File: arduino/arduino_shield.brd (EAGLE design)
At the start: 100 x 80 mm, 14 parts, among them IC3 PCF8574T, IC4 PCF8574T

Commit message: Board erstellt
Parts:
- removed C1: (no value), rcl:C0805
- removed JP6: (no value), pinheader_250:1X10
- added LED1, LED2, LED3: (no value), adafruit:CHIP-LED0805
- added R3, R4, R5: (no value), resistor:R0805
- added SG1: F/HGP, buzzer:F/HGP
- added U$1: (no value), frames:A4L-LOC
- JP1: value (none) -> POWERCON; device pinheader_250:1X03 -> PowerCon:AYAB_POW
- JP5: device pinheader_250:1X05 -> pinheader_250:1X10
- moved JP1 59.7 mm to (14.0, 21.6), turned to 90 degrees
- moved R1 37.6 mm to (41.3, 21.3), flipped to the bottom, turned to 270 degrees
- moved R2 35.2 mm to (41.3, 25.4), flipped to the bottom, turned to 90 degrees
- moved IC4 15.4 mm to (54.0, 26.0), flipped to the bottom, turned to 90 degrees
- moved JP3 14.7 mm to (53.3, 49.2)
- moved IC2 14.5 mm to (54.6, 40.6)
- moved IC3 13.0 mm to (29.2, 26.0), flipped to the bottom, turned to 90 degrees
- moved JP4 12.4 mm to (26.0, 49.2)
- moved IC1 12.1 mm to (29.8, 40.6)
- moved ARD1 8.89 mm to (8.89, 14.0)
- moved JP5 8.89 mm to (72.4, 35.6), turned to 270 degrees
- moved JP2 4.13 mm to (64.8, 21.3), turned to 180 degrees
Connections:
- net EOL_R renamed EOL0L
- removed net 5V: ARD1.5V
- removed net AREF: ARD1.AREF
- removed net EOL_L: ARD1.AIN0, JP1.1
- removed net GND1: ARD1.GND@1, ARD1.GND@2, ARD1.GND@3, C1.2, IC1.9, IC2.9, IC3.1, IC3.2, IC3.3, IC3.8, IC4.2, IC4.3, IC4.8, JP1.2, JP2.2, JP5.4, JP6.7
- removed net INT0: ARD1.2
- removed net INT1: ARD1.3
- removed net V+: IC1.10, IC2.10, JP4.1, JP4.2, JP6.10
- new net +15V: IC1.10, IC2.10, JP1.P$1, JP4.1, JP4.2
- new net +5V/1: JP1.P$4
- new net ENC0PINA: ARD1.2, JP5.4
- new net ENC0PINB: ARD1.3, JP5.5
- new net ENC0PINC: ARD1.4, JP5.6
- new net EOL0R: ARD1.AIN0, JP5.8
- new net GND: ARD1.GND@1, ARD1.GND@2, ARD1.GND@3, IC1.9, IC2.9, IC3.1, IC3.2, IC3.3, IC3.8, IC4.2, IC4.3, IC4.8, JP1.P$2, JP1.P$3, JP2.2, JP5.10, JP5.2, JP5.7, JP5.9, LED1.C
- new net N$33: LED1.A, R3.1
- new net N$34: ARD1.9, SG1.1
- new net N$35: ARD1.6, LED3.C
- new net N$36: ARD1.5, LED2.C
- new net N$37: LED3.A, R4.2
- new net N$38: LED2.A, R5.2
- net +5V: now also ARD1.5V, ARD1.AREF, IC4.1, JP5.1, R3.2, R4.1, R5.1, SG1.2; no longer C1.1, JP1.3, JP5.5, JP6.3
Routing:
- net +15V: track 0.00 -> 82.1 mm
- net SCL: track 0.00 -> 49.5 mm
- net GND: track 0.00 -> 48.2 mm, vias 0 -> 1
- net SDA: track 0.00 -> 46.3 mm
- net N$34: track 0.00 -> 36.2 mm
- net ENC0PINC: track 0.00 -> 35.4 mm
- net ENC0PINB: track 0.00 -> 31.8 mm
- net ENC0PINA: track 0.00 -> 28.1 mm
- net EOL0R: track 0.00 -> 23.4 mm
- net N$2: track 0.00 -> 15.1 mm
- net N$1: track 0.00 -> 15.1 mm
- net N$16: track 0.00 -> 14.1 mm
- net N$9: track 0.00 -> 14.1 mm
- net N$3: track 0.00 -> 13.9 mm
- net N$10: track 0.00 -> 13.9 mm
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- added copper zone on layer 16, net +5V
- added copper zone on layer 1, net GND
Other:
- board size 100 x 80 mm -> 69.2 x 54 mm

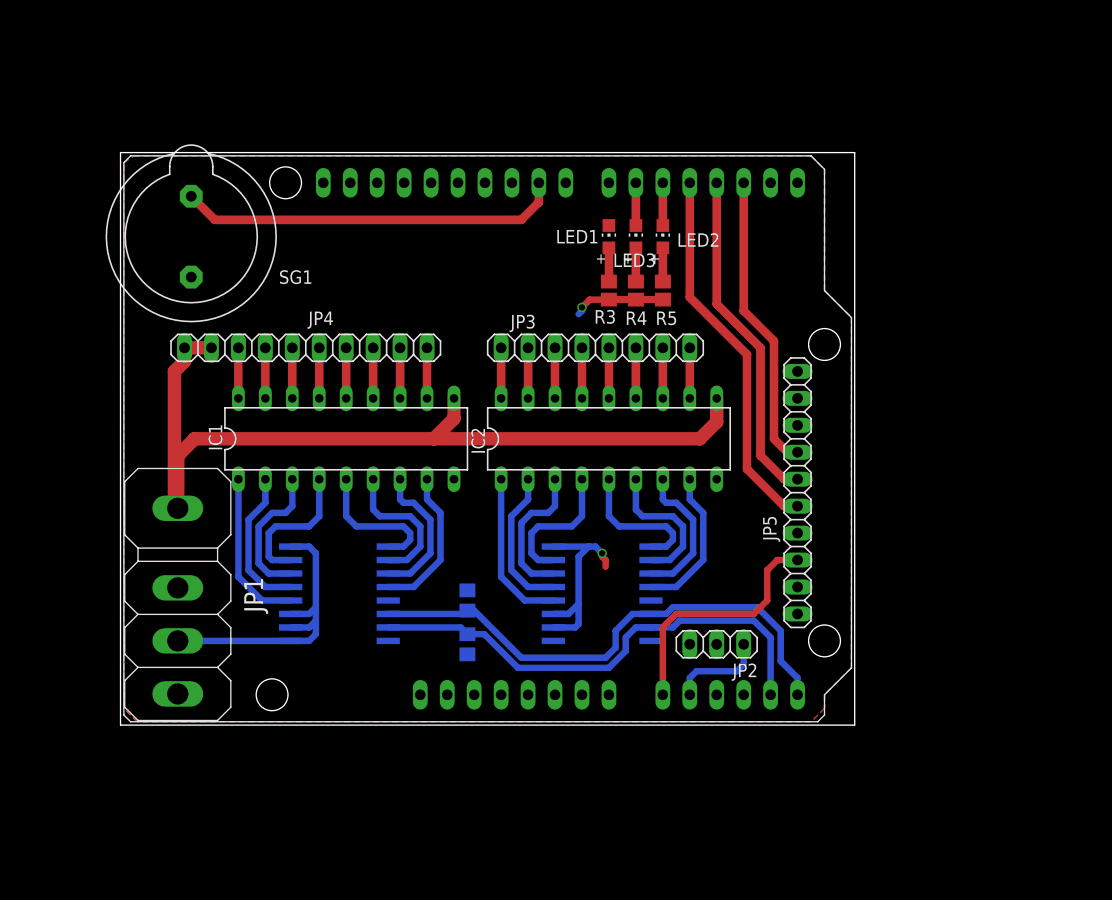
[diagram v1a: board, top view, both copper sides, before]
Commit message: Pinheader auf 2.5, Summer gändert, Beschriftung
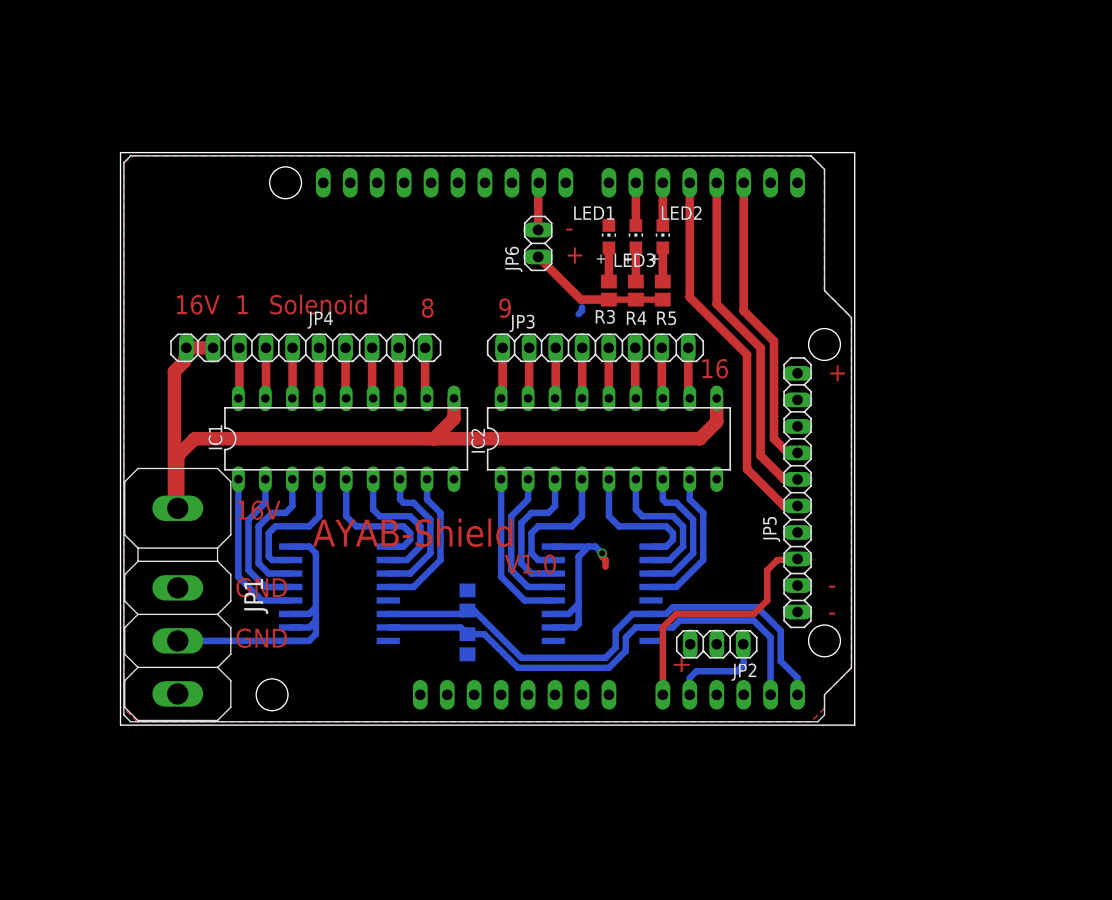
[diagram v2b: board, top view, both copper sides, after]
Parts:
- removed SG1: F/HGP, buzzer:F/HGP
- added JP6: (no value), pinhead:1X02
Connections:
- net +5V: now also JP6.1; no longer SG1.2
- net N$34: now also JP6.2; no longer SG1.1
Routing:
- net N$34: track 36.2 -> 4.47 mm
- net +5V: track 13.8 -> 14.2 mm, vias 1 -> 0
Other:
- board text added: "+"
- board text added: "-"
- board text added: "1"
- board text added: "16"
- board text added: "16V"
- board text added: "8"
- board text added: "9"
- board text added: "AYAB-Shield"
- board text added: "GND"
- board text added: "Solenoid"
- board text added: "V1.0"

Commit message: Qt Project entfernt
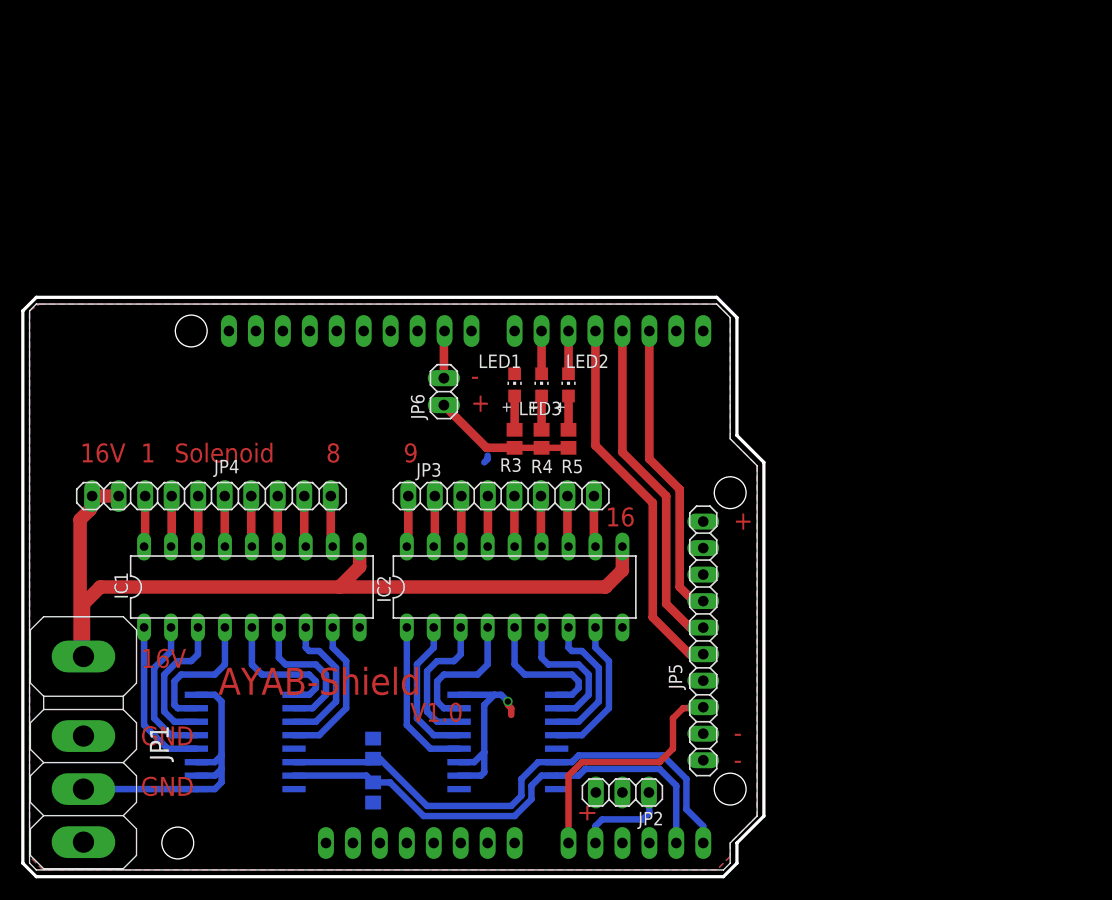
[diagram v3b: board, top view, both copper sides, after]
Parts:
- moved ARD1 16.6 mm to (0.00, 0.00)
- moved IC1 16.6 mm to (21.0, 26.7)
- moved IC2 16.6 mm to (45.7, 26.7)
- moved IC3 16.6 mm to (20.3, 12.1)
- moved IC4 16.6 mm to (45.1, 12.1)
- moved JP1 16.6 mm to (5.08, 7.62)
- moved JP3 16.6 mm to (44.5, 35.2)
- moved JP4 16.6 mm to (17.1, 35.2)
- moved JP5 16.6 mm to (63.5, 21.6)
- moved JP6 16.6 mm to (39.1, 45.1)
- moved LED1 16.6 mm to (45.7, 45.7)
- moved LED2 16.6 mm to (50.8, 45.7)
- moved LED3 16.6 mm to (48.3, 45.7)
- moved R1 16.6 mm to (32.4, 7.30)
- moved R2 16.6 mm to (32.4, 11.4)
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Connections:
- removed net IOREF: ARD1.IOREF
- net +5V: now also ARD1.IOREF
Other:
- board size 69.2 x 54 mm -> 69.9 x 54.6 mm
